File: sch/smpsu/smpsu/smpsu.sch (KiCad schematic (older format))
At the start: 8 parts, among them U1 LM2596S-3.3

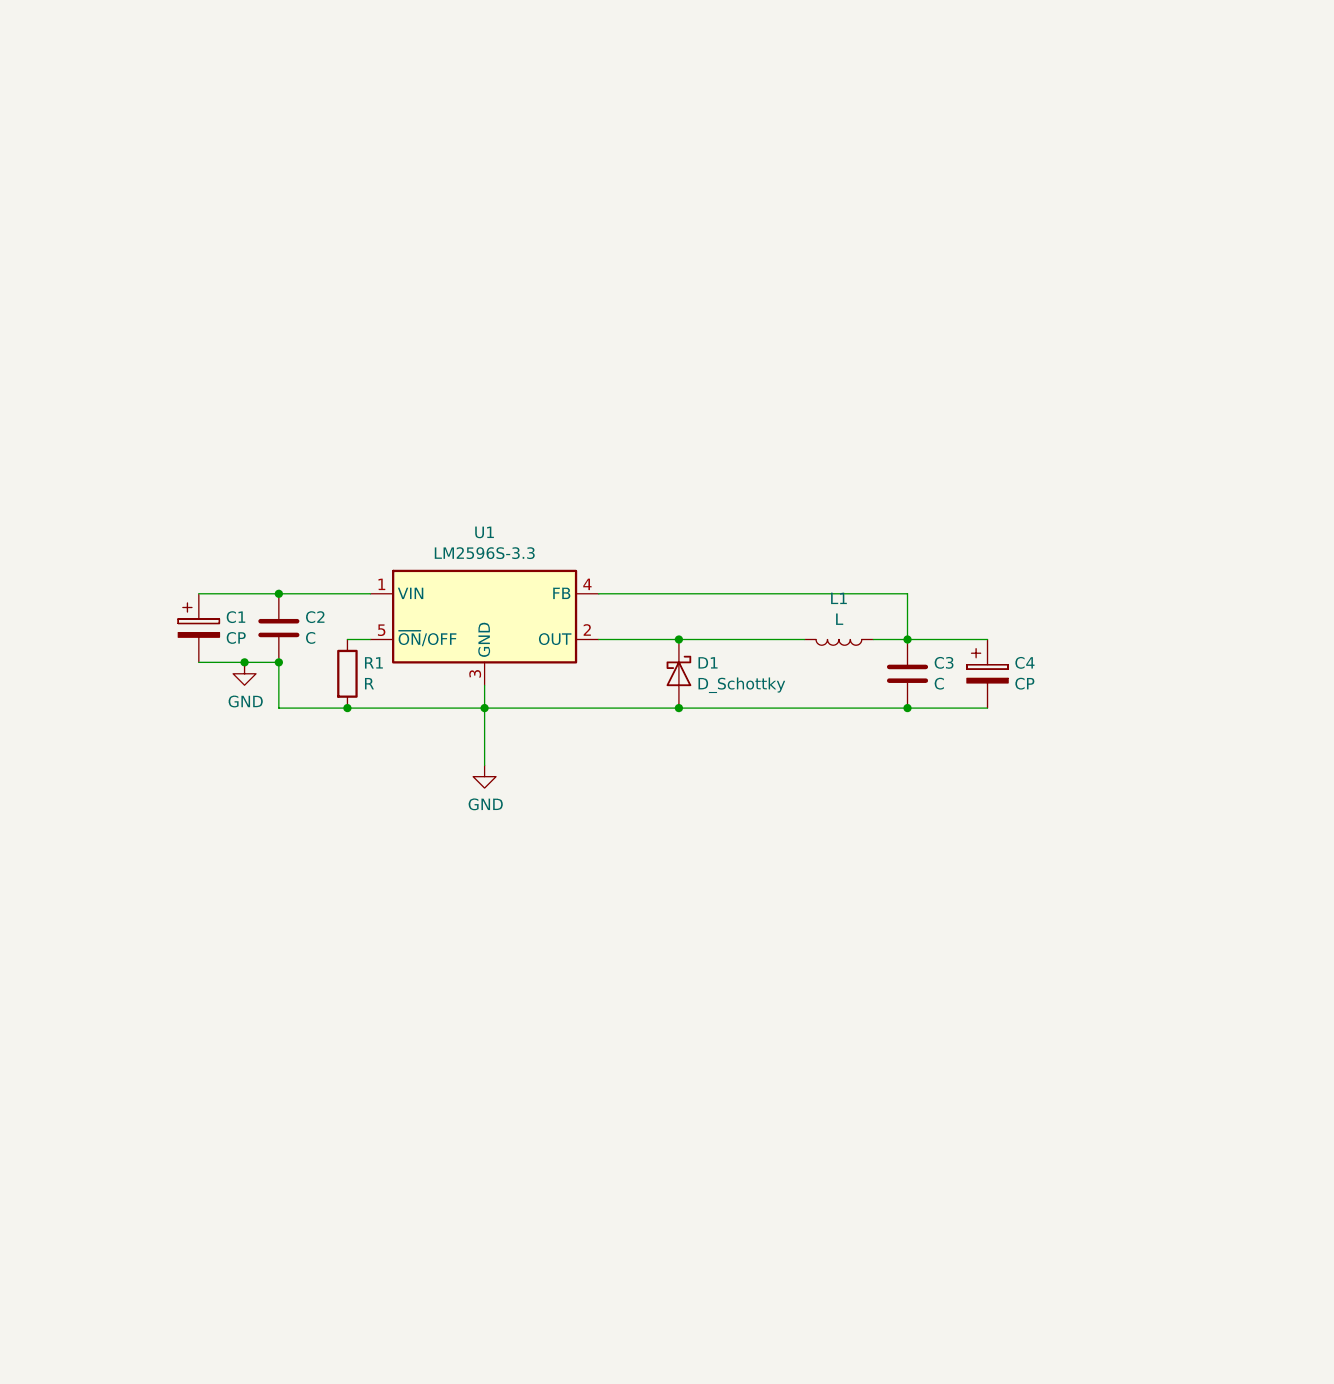
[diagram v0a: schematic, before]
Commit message: First version of switch mode psu/emi generator
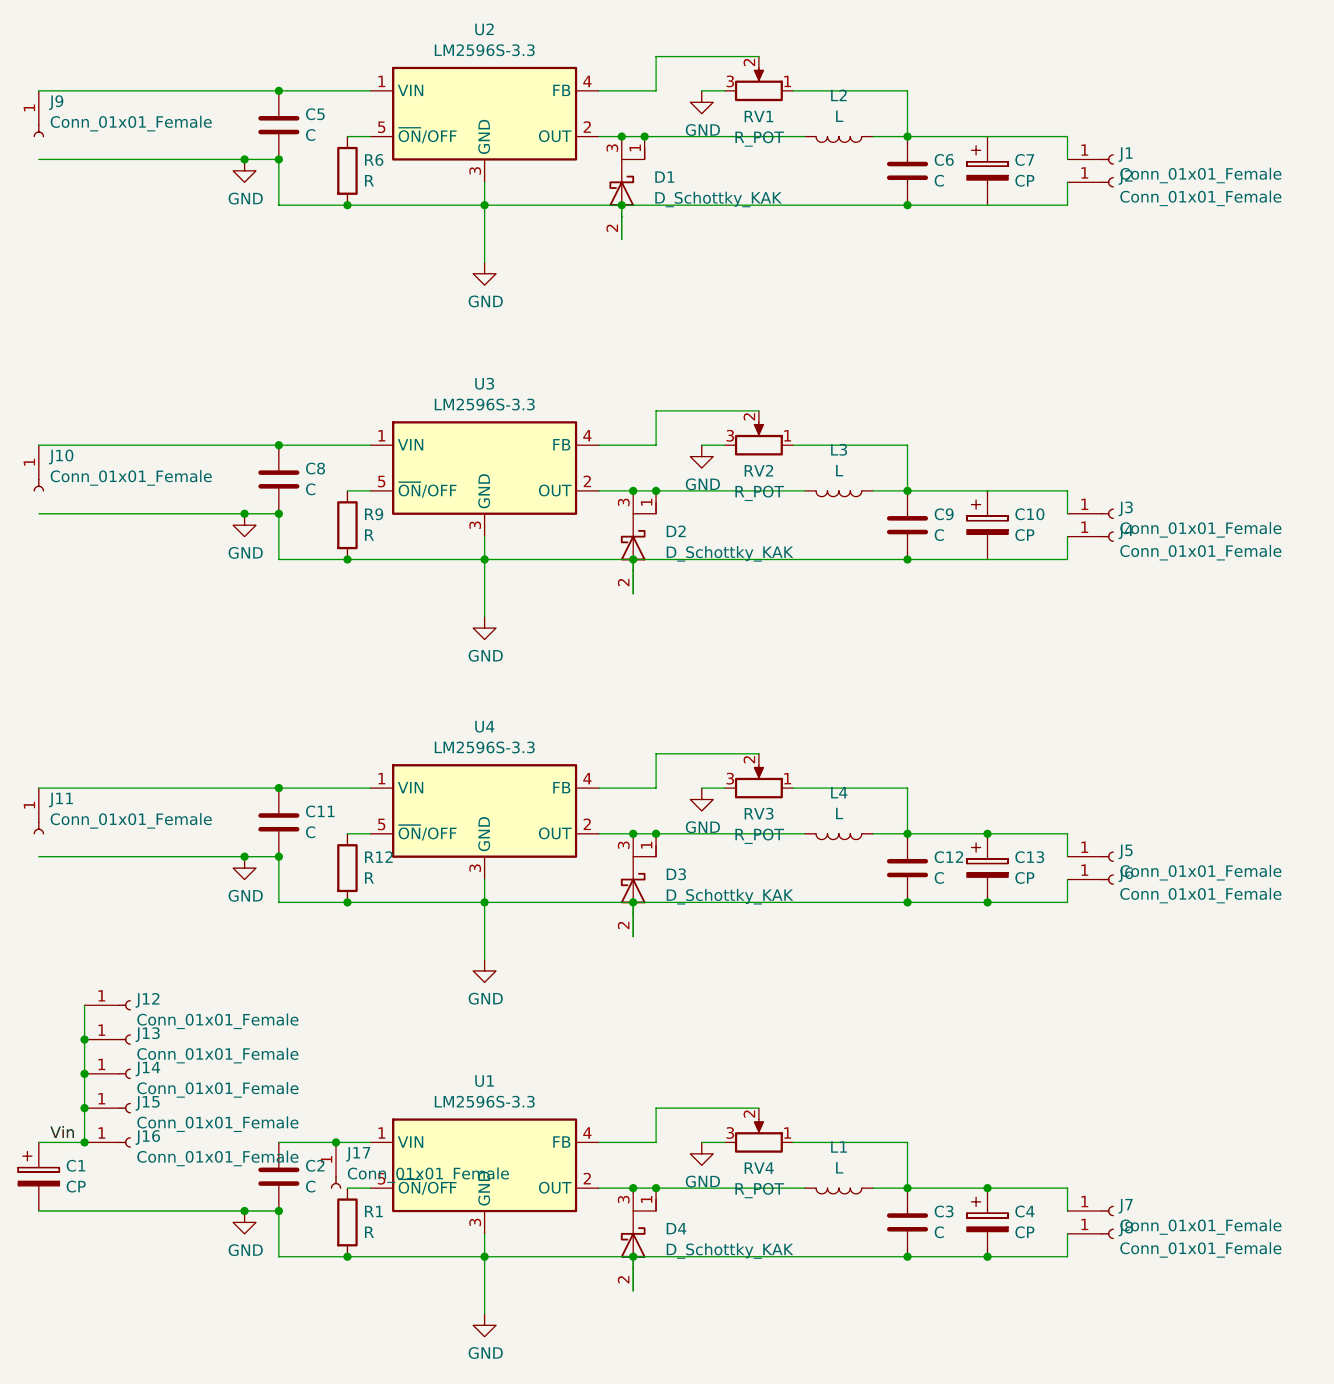
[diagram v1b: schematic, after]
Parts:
- removed D1: D_Schottky, TO_SOT_Packages_THT:TO-220-2_Vertical, symbol Device:D_Schottky
- added C10, C13, C7: CP, Capacitors_ThroughHole:CP_Radial_D10.0mm_P3.50mm, symbol Device:CP
- added C11, C12, C5, C6, C8, C9: C, Resistors_SMD:R_0805_HandSoldering, symbol Device:C
- added D1, D2, D3, D4: D_Schottky_KAK, TO_SOT_Packages_THT:TO-220-3_Vertical, symbol Device:D_Schottky_KAK
- added J1, J10, J11, J12, J13, J14, J15, J16, J17, J2, J3, J4, J5, J6, J7, J8, J9: Conn_01x01_Female, Wire_Pads:SolderWirePad_single_0-8mmDrill, symbol Connector:Conn_01x01_Female
- added L2, L3, L4: L, footprints_smpsu:Choke_Toroid_12x16mm_Vertical, symbol Device:L
- added R12, R6, R9: R, Resistors_SMD:R_0805_HandSoldering, symbol Device:R
- added RV1, RV2, RV3, RV4: R_POT, Potentiometers:Potentiometer_Trimmer_Bourns_3214J, symbol Device:R_POT
- added U2, U3, U4: LM2596S-3.3, TO_SOT_Packages_SMD:TO-263-5_TabPin3, symbol Regulator_Switching:LM2596S-3.3
- C1: footprint (none) -> Capacitors_ThroughHole:CP_Radial_D18.0mm_P7.50mm
- C4: footprint (none) -> Capacitors_ThroughHole:CP_Radial_D10.0mm_P3.50mm
- L1: footprint Choke_Toroid_ThroughHole:Transformer_Toroid_horizontal_Diameter18mm -> footprints_smpsu:Choke_Toroid_12x16mm_Vertical
- U1: footprint Package_TO_SOT_SMD:TO-263-5_TabPin3 -> TO_SOT_Packages_SMD:TO-263-5_TabPin3
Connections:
- net GND: now also C10.2, C11.2, C12.2, C13.2, C5.2, C6.2, C7.2, C8.2, C9.2, D1.2 (A), D2.2 (A), D3.2 (A), D4.2 (A), J2.1 (Pin_1), J4.1 (Pin_1), J6.1 (Pin_1), J8.1 (Pin_1), R12.2, R6.2, R9.2, RV1.3, RV2.3, RV3.3, RV4.3, U2.3 (GND), U3.3 (GND), U4.3 (GND)
- net at C2.1, U1.1 (VIN): now also J17.1 (Pin_1); no longer C1.1
- net at L1.2, U1.2 (OUT): now also D4.1 (K), D4.3 (K)
- net at C3.1, C4.1, L1.1: now also J7.1 (Pin_1), RV4.1; no longer U1.4 (FB)
- new net: RV4.2, U1.4 (FB)
- new net: C11.1, J11.1 (Pin_1), U4.1 (VIN)
- new net: D3.1 (K), D3.3 (K), L4.2, U4.2 (OUT)
- new net: RV3.2, U4.4 (FB)
- new net: R12.1, U4.5 (~ON~/OFF)
- new net: C12.1, C13.1, J5.1 (Pin_1), L4.1, RV3.1
- new net: C8.1, J10.1 (Pin_1), U3.1 (VIN)
- new net: D2.1 (K), D2.3 (K), L3.2, U3.2 (OUT)
- new net: RV2.2, U3.4 (FB)
- new net: R9.1, U3.5 (~ON~/OFF)
- new net: C10.1, C9.1, J3.1 (Pin_1), L3.1, RV2.1
- new net: C5.1, J9.1 (Pin_1), U2.1 (VIN)
- new net: D1.1 (K), D1.3 (K), L2.2, U2.2 (OUT)
- new net: RV1.2, U2.4 (FB)
- new net: R6.1, U2.5 (~ON~/OFF)
- new net: C6.1, C7.1, J1.1 (Pin_1), L2.1, RV1.1
- new net Vin: C1.1, J12.1 (Pin_1), J13.1 (Pin_1), J14.1 (Pin_1), J15.1 (Pin_1), J16.1 (Pin_1)
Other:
- moved on the sheet: C1, C2, C3, C4, L1, R1, U1

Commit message: Added smpsu test schematic and gerbers
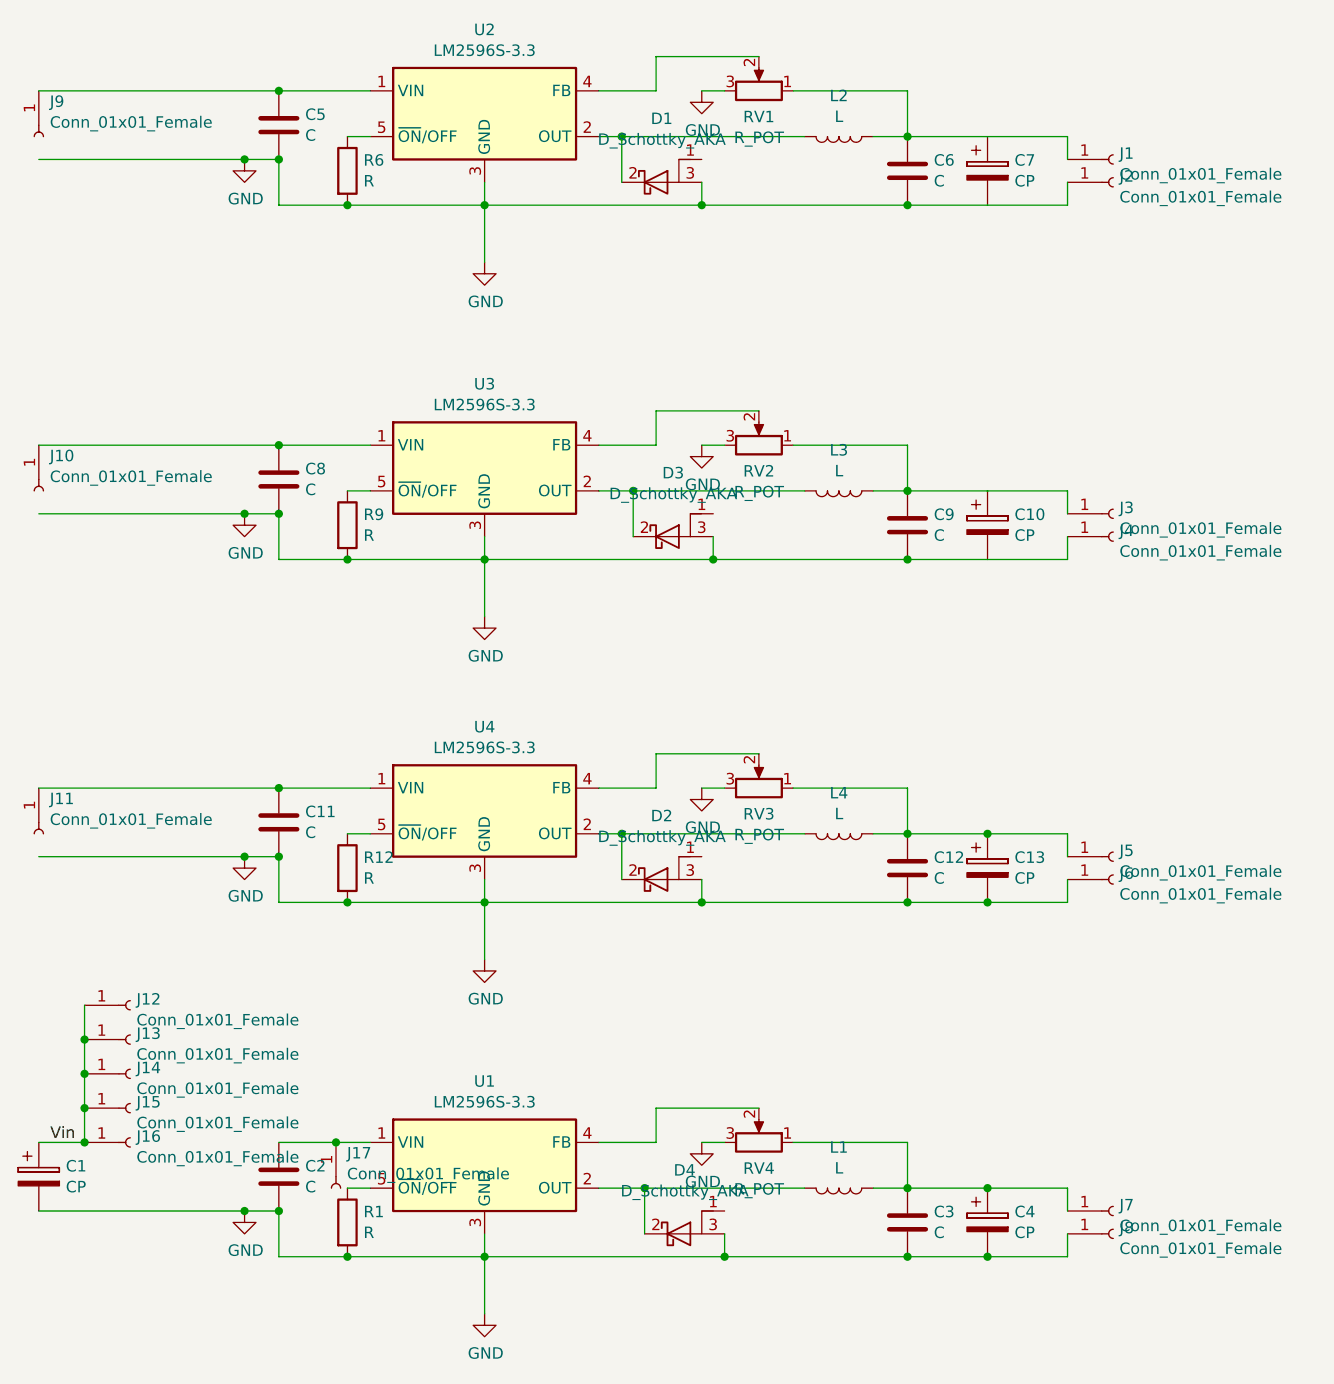
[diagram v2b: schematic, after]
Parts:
- removed D1, D2, D3, D4: D_Schottky_KAK, TO_SOT_Packages_THT:TO-220-3_Vertical, symbol Device:D_Schottky_KAK
- added D1, D2, D3, D4: D_Schottky_AKA, TO_SOT_Packages_THT:TO-220-3_Vertical, symbol Device:D_Schottky_AKA
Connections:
- net GND: now also D1.3 (A), D2.3 (A), D3.3 (A), D4.3 (A)
- net at L1.2, U1.2 (OUT): now also D4.2 (K)
- net at L4.2, U4.2 (OUT): now also D2.2 (K)
- net at L3.2, U3.2 (OUT): now also D3.2 (K)
- net at L2.2, U2.2 (OUT): now also D1.2 (K)
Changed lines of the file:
@@
 Text Label 700  6200 0    50   ~ 0
 Vin
-$Comp
-L Device:D_Schottky_KAK D3
-U 1 1 5CFA2ABB
-P 3250 5100
-F 0 "D3" V 3179 5240 50  0000 L CNN
-F 1 "D_Schottky_KAK" V 3270 5240 50  0000 L CNN
-F 2 "TO_SOT_Packages_THT:TO-220-3_Vertical" H 3250 5100 50  0001 C CNN
-F 3 "~" H 3250 5100 50  0001 C CNN
-	1    3250 5100
-	0    1    1    0
-$EndComp
-Wire Wire Line
-	3100 6400 3250 6400
-Wire Wire Line
-	2600 6700 3250 6700
-Wire Wire Line
-	3100 4850 3250 4850
-Wire Wire Line
-	2600 5150 3250 5150
-Wire Wire Line
-	3100 3350 3250 3350
-Wire Wire Line
-	2600 3650 3250 3650
-Wire Wire Line
-	3100 1800 3200 1800
-Wire Wire Line
-	2600 2100 3200 2100
-$Comp
-L Device:D_Schottky_KAK D4
-U 1 1 5CFA34A7
-P 3250 6650
-F 0 "D4" V 3179 6790 50  0000 L CNN
-F 1 "D_Schottky_KAK" V 3270 6790 50  0000 L CNN
-F 2 "TO_SOT_Packages_THT:TO-220-3_Vertical" H 3250 6650 50  0001 C CNN
-F 3 "~" H 3250 6650 50  0001 C CNN
-	1    3250 6650
-	0    1    1    0
-$EndComp
-Wire Wire Line
-	3350 6400 4000 6400
-Wire Wire Line
-	3350 4850 4000 4850
-$Comp
-L Device:D_Schottky_KAK D2
-U 1 1 5CFA3654
-P 3250 3600
-F 0 "D2" V 3179 3740 50  0000 L CNN
-F 1 "D_Schottky_KAK" V 3270 3740 50  0000 L CNN
-F 2 "TO_SOT_Packages_THT:TO-220-3_Vertical" H 3250 3600 50  0001 C CNN
-F 3 "~" H 3250 3600 50  0001 C CNN
-	1    3250 3600
-	0    1    1    0
-$EndComp
-Wire Wire Line
-	3350 3350 4000 3350
-$Comp
-L Device:D_Schottky_KAK D1
-U 1 1 5CFA36D4
-P 3200 2050
-F 0 "D1" V 3129 2190 50  0000 L CNN
-F 1 "D_Schottky_KAK" V 3220 2190 50  0000 L CNN
-F 2 "TO_SOT_Packages_THT:TO-220-3_Vertical" H 3200 2050 50  0001 C CNN
-F 3 "~" H 3200 2050 50  0001 C CNN
-	1    3200 2050
-	0    1    1    0
-$EndComp
-Wire Wire Line
-	3300 1800 4000 1800
-Wire Wire Line
-	3300 1800 3200 1800
-Connection ~ 3300 1800
-Connection ~ 3200 1800
-Wire Wire Line
-	3200 2250 3200 2100
-Connection ~ 3200 2100
-Wire Wire Line
-	3200 2100 4450 2100
-Wire Wire Line
-	3250 3350 3350 3350
-Connection ~ 3250 3350
-Connection ~ 3350 3350
-Wire Wire Line
-	3250 3800 3250 3650
-Connection ~ 3250 3650
-Wire Wire Line
-	3250 3650 4450 3650
-Wire Wire Line
-	3250 4850 3350 4850
-Connection ~ 3250 4850
-Connection ~ 3350 4850
-Wire Wire Line
-	3250 5300 3250 5150
-Connection ~ 3250 5150
-Wire Wire Line
-	3250 5150 4450 5150
-Wire Wire Line
-	3250 6400 3350 6400
-Connection ~ 3250 6400
-Connection ~ 3350 6400
-Wire Wire Line
-	3250 6850 3250 6700
-Connection ~ 3250 6700
-Wire Wire Line
-	3250 6700 4450 6700
 Wire Wire Line
 	5150 6500 5150 6400
@@
 	0    1    1    0
 $EndComp
+$Comp
+L Device:D_Schottky_AKA D4
+U 1 1 5D100253
+P 3450 6600
+F 0 "D4" H 3475 6878 50  0000 C CNN
+F 1 "D_Schottky_AKA" H 3475 6787 50  0000 C CNN
+F 2 "TO_SOT_Packages_THT:TO-220-3_Vertical" H 3450 6600 50  0001 C CNN
+F 3 "~" H 3450 6600 50  0001 C CNN
+	1    3450 6600
+	1    0    0    -1
+$EndComp
+Wire Wire Line
+	3100 6400 3300 6400
+Wire Wire Line
+	2600 6700 3650 6700
+Wire Wire Line
+	3650 6600 3650 6700
+Connection ~ 3650 6700
+Wire Wire Line
+	3650 6700 4450 6700
+Wire Wire Line
+	3300 6600 3300 6400
+Connection ~ 3300 6400
+Wire Wire Line
+	3300 6400 4000 6400
+Wire Wire Line
+	3100 4850 3200 4850
+Wire Wire Line
+	3100 3350 3250 3350
+Wire Wire Line
+	2600 3650 3600 3650
+Wire Wire Line
+	3100 1800 3200 1800
+Wire Wire Line
+	2600 2100 3550 2100
+$Comp
+L Device:D_Schottky_AKA D2
+U 1 1 5D10D9F6
+P 3350 5050
+F 0 "D2" H 3375 5328 50  0000 C CNN
+F 1 "D_Schottky_AKA" H 3375 5237 50  0000 C CNN
+F 2 "TO_SOT_Packages_THT:TO-220-3_Vertical" H 3350 5050 50  0001 C CNN
+F 3 "~" H 3350 5050 50  0001 C CNN
+	1    3350 5050
+	1    0    0    -1
+$EndComp
+$Comp
+L Device:D_Schottky_AKA D3
+U 1 1 5D10DA9E
+P 3400 3550
+F 0 "D3" H 3425 3828 50  0000 C CNN
+F 1 "D_Schottky_AKA" H 3425 3737 50  0000 C CNN
+F 2 "TO_SOT_Packages_THT:TO-220-3_Vertical" H 3400 3550 50  0001 C CNN
+F 3 "~" H 3400 3550 50  0001 C CNN
+	1    3400 3550
+	1    0    0    -1
+$EndComp
+$Comp
+L Device:D_Schottky_AKA D1
+U 1 1 5D10DB7D
+P 3350 2000
+F 0 "D1" H 3375 2278 50  0000 C CNN
+F 1 "D_Schottky_AKA" H 3375 2187 50  0000 C CNN
+F 2 "TO_SOT_Packages_THT:TO-220-3_Vertical" H 3350 2000 50  0001 C CNN
+F 3 "~" H 3350 2000 50  0001 C CNN
+	1    3350 2000
+	1    0    0    -1
+$EndComp
+Wire Wire Line
+	3200 2000 3200 1800
+Connection ~ 3200 1800
+Wire Wire Line
+	3200 1800 4000 1800
+Wire Wire Line
+	3550 2000 3550 2100
+Connection ~ 3550 2100
+Wire Wire Line
+	3550 2100 4450 2100
+Wire Wire Line
+	3250 3550 3250 3350
+Connection ~ 3250 3350
+Wire Wire Line
+	3250 3350 4000 3350
+Wire Wire Line
+	3600 3550 3600 3650
+Connection ~ 3600 3650
+Wire Wire Line
+	3600 3650 4450 3650
+Wire Wire Line
+	3200 5050 3200 4850
+Connection ~ 3200 4850
+Wire Wire Line
+	3200 4850 4000 4850
+Wire Wire Line
+	3550 5050 3550 5150
+Wire Wire Line
+	2600 5150 3550 5150
+Connection ~ 3550 5150
+Wire Wire Line
+	3550 5150 4450 5150
 $EndSCHEMATC
